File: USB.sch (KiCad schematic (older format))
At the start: 14 parts, among them J201 MICROUSB-TH, J202 CONN_01X02, J203 MICROUSB-TH, J204 USB_A_TH

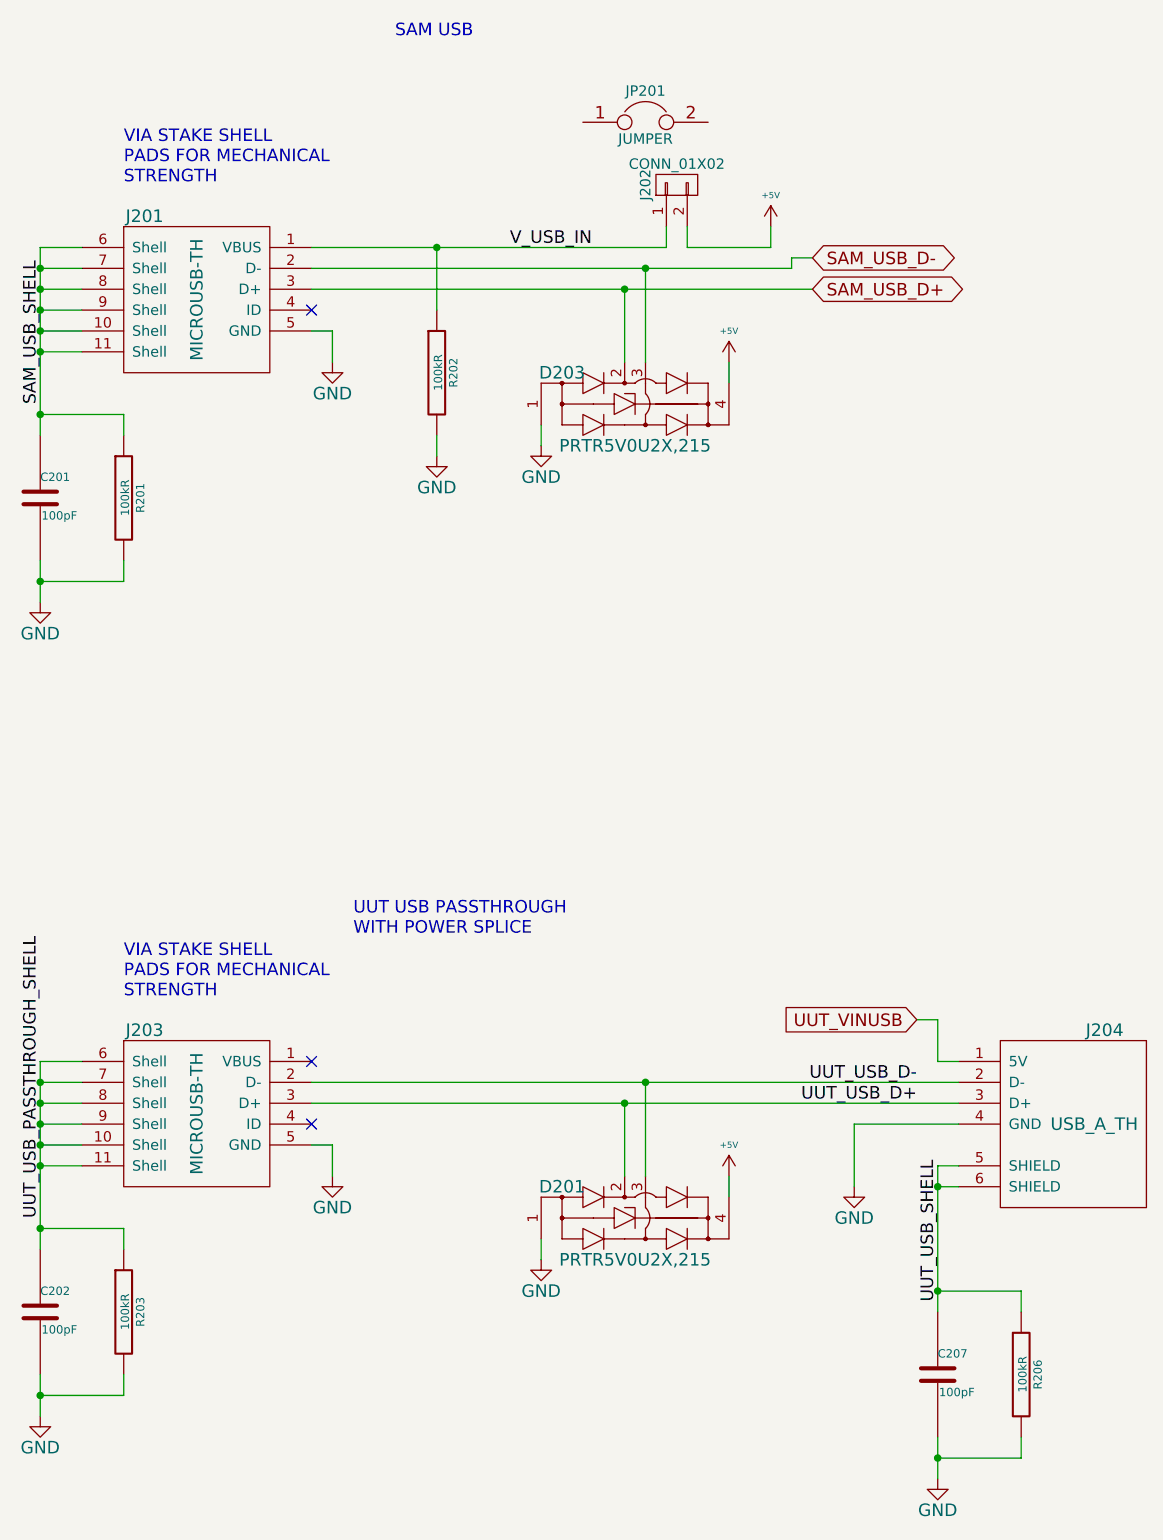
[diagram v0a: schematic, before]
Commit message: usb port and barrel jack tweaks
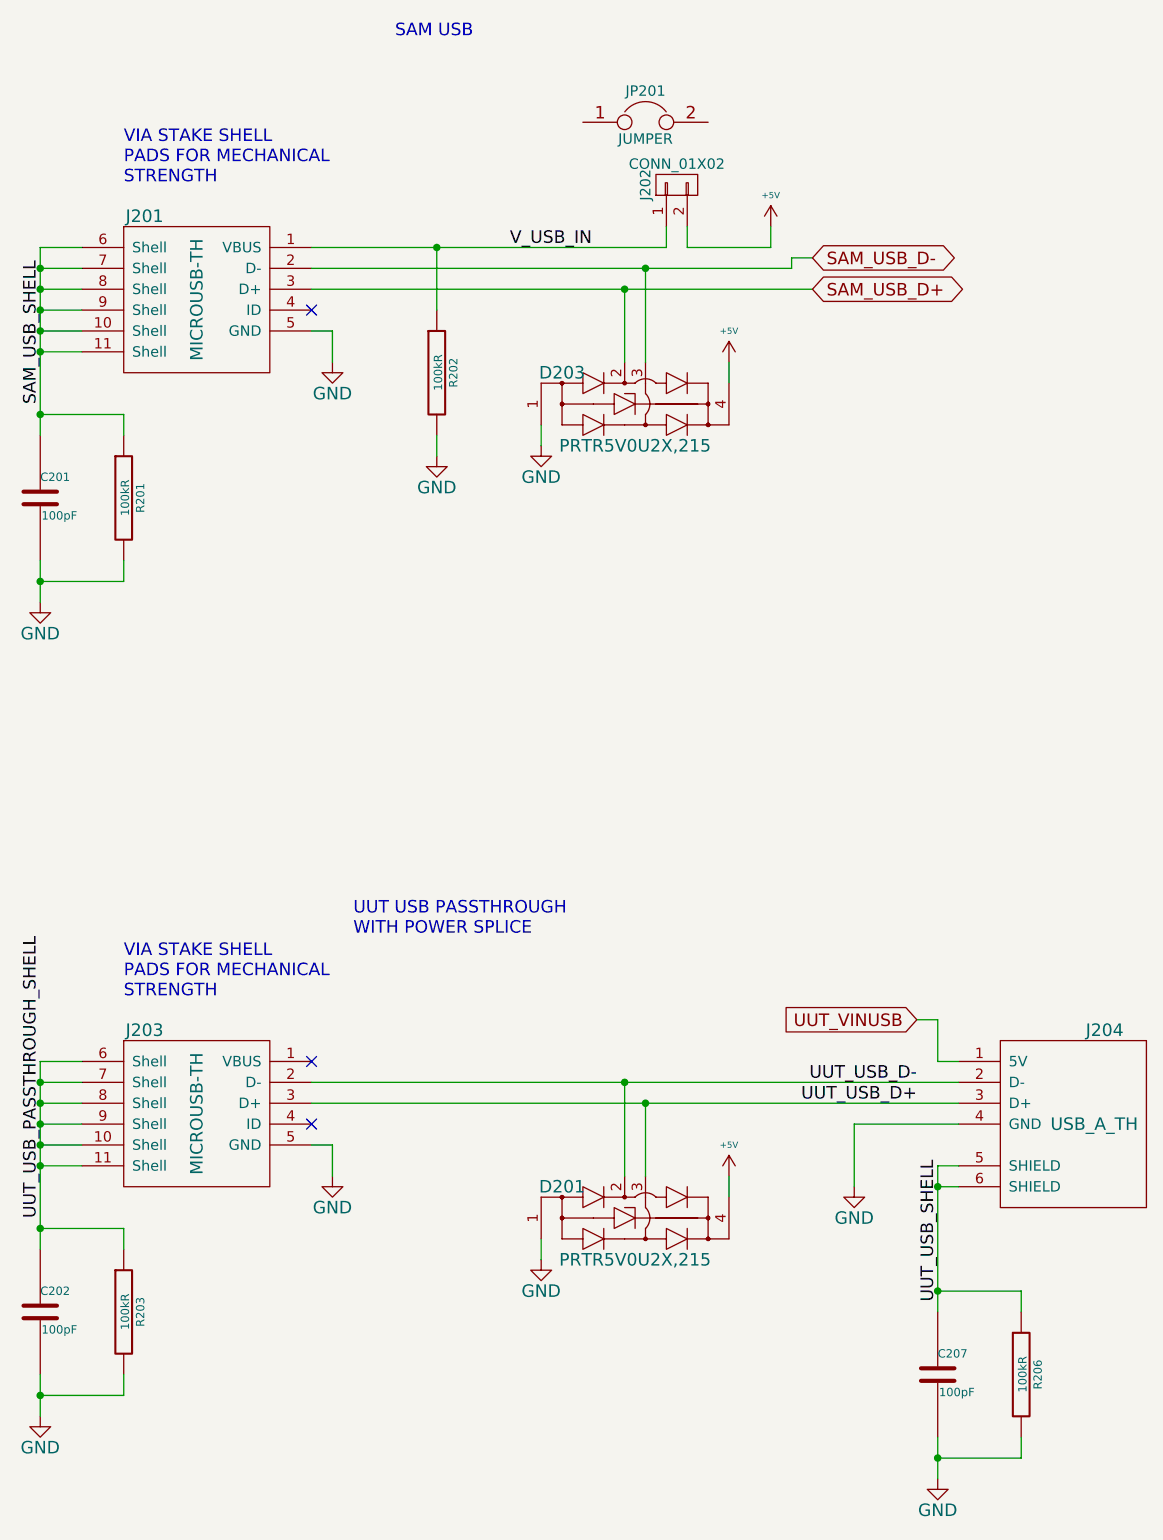
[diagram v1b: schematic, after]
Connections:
- net UUT_USB_D+: now also D201.3; no longer D201.2
- net UUT_USB_D-: now also D201.2; no longer D201.3
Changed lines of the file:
@@
 	7100 3100 7200 3100
 Wire Wire Line
-	7100 2700 8800 2700
-Wire Wire Line
-	7100 2800 9400 2800
-Wire Wire Line
-	7100 2900 9500 2900
+	7100 2700 7700 2700
+Wire Wire Line
+	7700 2700 8800 2700
+Wire Wire Line
+	7100 2800 8700 2800
+Wire Wire Line
+	8700 2800 9400 2800
+Wire Wire Line
+	7100 2900 8600 2900
+Wire Wire Line
+	8600 2900 9500 2900
 Connection ~ 8600 2900
 Wire Wire Line
@@
 	6200 3500 5800 3500
 Wire Wire Line
-	5800 2700 5800 3600
-Wire Wire Line
-	5800 4200 5800 4400
+	5800 2700 5800 2800
+Wire Wire Line
+	5800 2800 5800 2900
+Wire Wire Line
+	5800 2900 5800 3000
+Wire Wire Line
+	5800 3000 5800 3100
+Wire Wire Line
+	5800 3100 5800 3200
+Wire Wire Line
+	5800 3200 5800 3500
+Wire Wire Line
+	5800 3500 5800 3600
+Wire Wire Line
+	5800 4200 5800 4300
+Wire Wire Line
+	5800 4300 5800 4400
 Wire Wire Line
 	6200 4200 6200 4300
@@
 	10500 7700 10100 7700
 Wire Wire Line
-	10100 7100 10100 7800
-Wire Wire Line
-	10100 8400 10100 8600
+	10100 7100 10100 7200
+Wire Wire Line
+	10100 7200 10100 7700
+Wire Wire Line
+	10100 7700 10100 7800
+Wire Wire Line
+	10100 8400 10100 8500
+Wire Wire Line
+	10100 8500 10100 8600
 Wire Wire Line
 	10500 8400 10500 8500
@@
 Text Notes 6200 6300 0    60   ~ 0
 VIA STAKE SHELL\nPADS FOR MECHANICAL\nSTRENGTH
-Connection ~ 8700 6700
-Wire Wire Line
-	8700 7150 8700 6700
+Connection ~ 8600 6700
+Wire Wire Line
+	8600 7150 8600 6700
 Wire Wire Line
 	7200 7000 7200 7150
@@
 	7100 7000 7200 7000
 Wire Wire Line
-	7100 6700 10200 6700
-Wire Wire Line
-	7100 6800 10200 6800
-Connection ~ 8600 6800
+	7100 6700 8600 6700
+Wire Wire Line
+	8600 6700 10200 6700
+Wire Wire Line
+	7100 6800 8700 6800
+Wire Wire Line
+	8700 6800 10200 6800
+Connection ~ 8700 6800
 Wire Wire Line
 	8200 7550 8200 7450
@@
 Connection ~ 5800 7100
 Wire Wire Line
-	8600 7150 8600 6800
+	8700 7150 8700 6800
 Wire Wire Line
 	6200 7500 6200 7400
@@
 	6200 7400 5800 7400
 Wire Wire Line
-	5800 6600 5800 7500
-Wire Wire Line
-	5800 8100 5800 8300
+	5800 6600 5800 6700
+Wire Wire Line
+	5800 6700 5800 6800
+Wire Wire Line
+	5800 6800 5800 6900
+Wire Wire Line
+	5800 6900 5800 7000
+Wire Wire Line
+	5800 7000 5800 7100
+Wire Wire Line
+	5800 7100 5800 7400
+Wire Wire Line
+	5800 7400 5800 7500
+Wire Wire Line
+	5800 8100 5800 8200
+Wire Wire Line
+	5800 8200 5800 8300
 Wire Wire Line
 	6200 8100 6200 8200

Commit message: still easier access to usb
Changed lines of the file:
@@
 	7100 3100 7200 3100
 Wire Wire Line
-	7100 2700 7700 2700
-Wire Wire Line
-	7700 2700 8800 2700
-Wire Wire Line
-	7100 2800 8700 2800
-Wire Wire Line
-	8700 2800 9400 2800
-Wire Wire Line
-	7100 2900 8600 2900
-Wire Wire Line
-	8600 2900 9500 2900
+	7100 2700 8800 2700
+Wire Wire Line
+	7100 2800 9400 2800
+Wire Wire Line
+	7100 2900 9500 2900
 Connection ~ 8600 2900
 Wire Wire Line
@@
 	6200 3500 5800 3500
 Wire Wire Line
-	5800 2700 5800 2800
-Wire Wire Line
-	5800 2800 5800 2900
-Wire Wire Line
-	5800 2900 5800 3000
-Wire Wire Line
-	5800 3000 5800 3100
-Wire Wire Line
-	5800 3100 5800 3200
-Wire Wire Line
-	5800 3200 5800 3500
-Wire Wire Line
-	5800 3500 5800 3600
-Wire Wire Line
-	5800 4200 5800 4300
-Wire Wire Line
-	5800 4300 5800 4400
+	5800 2700 5800 3600
+Wire Wire Line
+	5800 4200 5800 4400
 Wire Wire Line
 	6200 4200 6200 4300
@@
 	10500 7700 10100 7700
 Wire Wire Line
-	10100 7100 10100 7200
-Wire Wire Line
-	10100 7200 10100 7700
-Wire Wire Line
-	10100 7700 10100 7800
-Wire Wire Line
-	10100 8400 10100 8500
-Wire Wire Line
-	10100 8500 10100 8600
+	10100 7100 10100 7800
+Wire Wire Line
+	10100 8400 10100 8600
 Wire Wire Line
 	10500 8400 10500 8500
@@
 	7100 7000 7200 7000
 Wire Wire Line
-	7100 6700 8600 6700
-Wire Wire Line
-	8600 6700 10200 6700
-Wire Wire Line
-	7100 6800 8700 6800
-Wire Wire Line
-	8700 6800 10200 6800
+	7100 6700 10200 6700
+Wire Wire Line
+	7100 6800 10200 6800
 Connection ~ 8700 6800
 Wire Wire Line
@@
 	6200 7400 5800 7400
 Wire Wire Line
-	5800 6600 5800 6700
-Wire Wire Line
-	5800 6700 5800 6800
-Wire Wire Line
-	5800 6800 5800 6900
-Wire Wire Line
-	5800 6900 5800 7000
-Wire Wire Line
-	5800 7000 5800 7100
-Wire Wire Line
-	5800 7100 5800 7400
-Wire Wire Line
-	5800 7400 5800 7500
-Wire Wire Line
-	5800 8100 5800 8200
-Wire Wire Line
-	5800 8200 5800 8300
+	5800 6600 5800 7500
+Wire Wire Line
+	5800 8100 5800 8300
 Wire Wire Line
 	6200 8100 6200 8200
